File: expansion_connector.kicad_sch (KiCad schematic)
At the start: 18 parts, among them J18 ASP-218650-01_mounting_holes, J8 Plug_Samtec_UMPT_1x6_UMPT-06-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

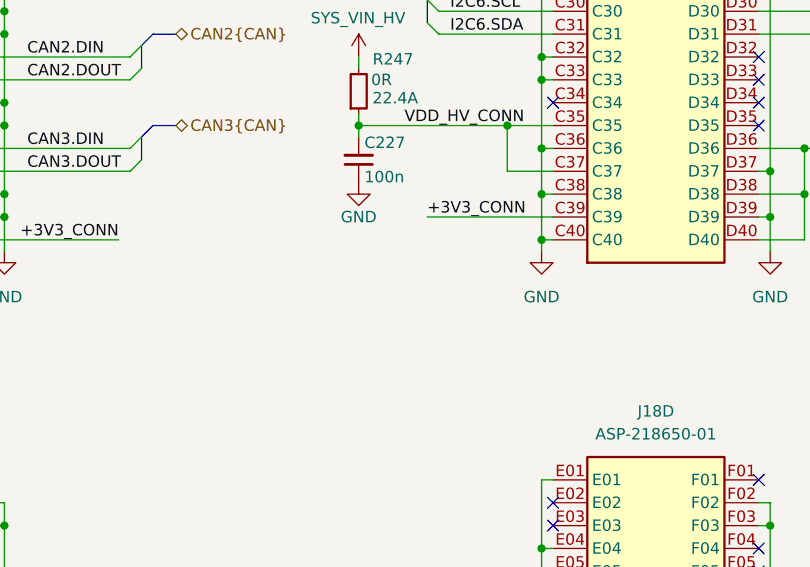
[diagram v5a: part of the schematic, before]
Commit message: [#83396] Implement small post review fixes eg. correct LED resistor values, update sheet table, delete four wire connections
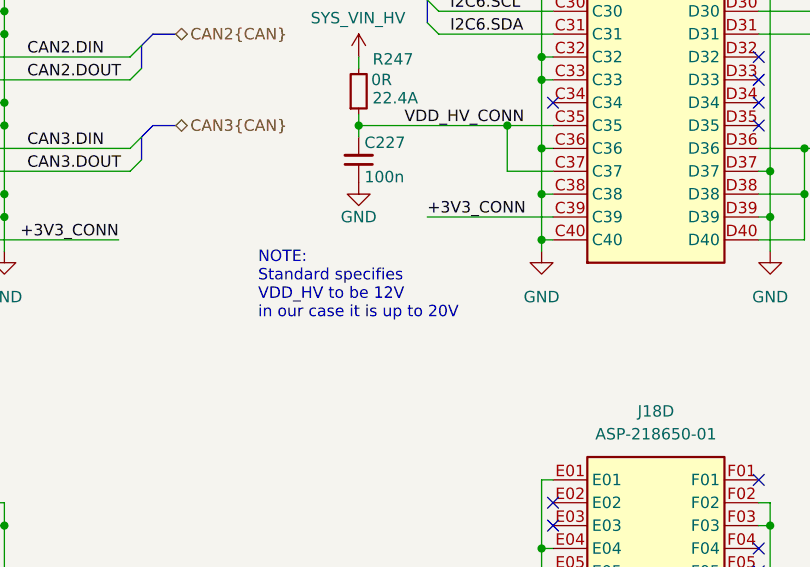
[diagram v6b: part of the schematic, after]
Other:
- note added: "NOTE: Standard specifies VDD_HV to be 12V in our case it is up to 20V"
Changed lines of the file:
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@@
+		)
+	)
+	(text "NOTE:\nStandard specifies\nVDD_HV to be 12V\nin our case it is up to 20V"
+		(exclude_from_sim no)
+		(at 141.224 142.24 0)
+		(effects
+			(font
+				(size 1.27 1.27)
+			)
+			(justify left)
 		)
 	)

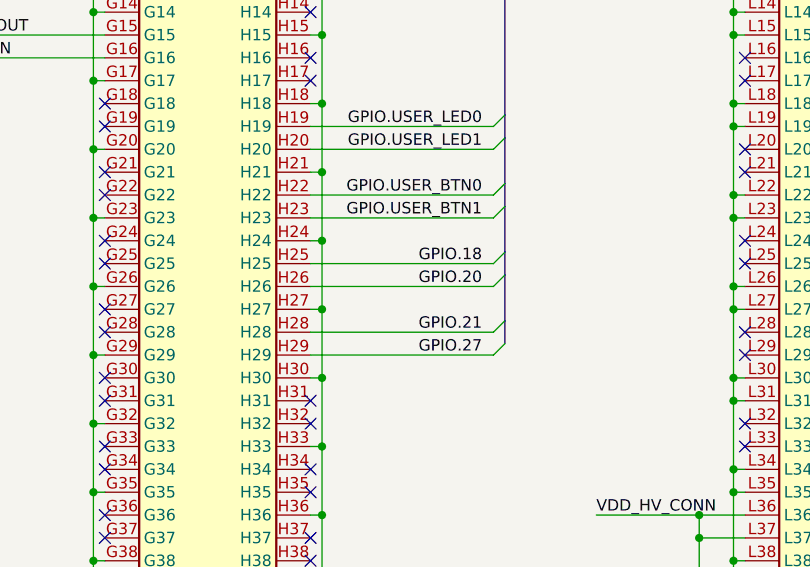
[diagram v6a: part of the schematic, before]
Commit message: [#83396] Continue post review fixes according power and M.2
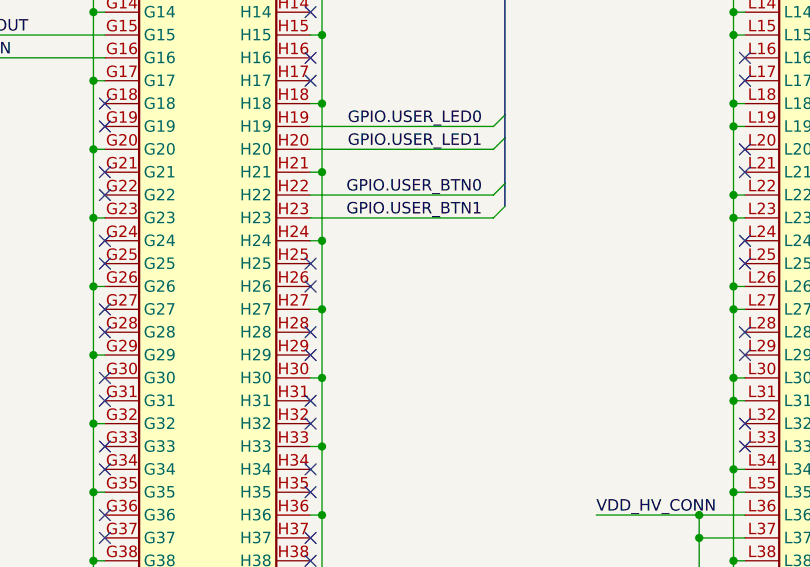
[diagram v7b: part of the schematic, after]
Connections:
- net GPIO.18: no longer names the net of J18.H25
- net GPIO.20: no longer names the net of J18.H26
- net GPIO.21: no longer names the net of J18.H28
- net GPIO.27: no longer names the net of J18.H29
- no-connect marks 201 -> 205
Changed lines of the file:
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@@
 	)
 	(no_connect
+		(at 294.64 99.06)
+	)
+	(no_connect
 		(at 271.78 168.91)
 	)
@@
 	)
 	(no_connect
+		(at 294.64 106.68)
+	)
+	(no_connect
 		(at 111.76 76.2)
 	)
@@
 	)
 	(no_connect
+		(at 294.64 101.6)
+	)
+	(no_connect
 		(at 271.78 207.01)
 	)
@@
 	)
 	(no_connect
+		(at 294.64 109.22)
+	)
+	(no_connect
 		(at 173.99 191.77)
 	)
@@
 	)
 	(bus_entry
-		(at 316.23 107.95)
-		(size -1.27 1.27)
-		(stroke
-			(width 0)
-			(type default)
-		)
-	)
-	(bus_entry
 		(at 215.9 233.68)
 		(size -1.27 1.27)
@@
 	)
 	(bus_entry
-		(at 316.23 105.41)
-		(size -1.27 1.27)
-		(stroke
-			(width 0)
-			(type default)
-		)
-	)
-	(bus_entry
 		(at 250.19 57.15)
 		(size 1.27 1.27)
@@
 	)
 	(bus_entry
-		(at 316.23 97.79)
-		(size -1.27 1.27)
-		(stroke
-			(width 0)
-			(type default)
-		)
-	)
-	(bus_entry
 		(at 134.62 64.77)
 		(size -1.27 1.27)
@@
 	)
 	(bus_entry
-		(at 316.23 100.33)
-		(size -1.27 1.27)
-		(stroke
-			(width 0)
-			(type default)
-		)
-	)
-	(bus_entry
 		(at 35.56 123.19)
 		(size 1.27 1.27)
@@
 		)
 	)
-	(bus
-		(pts
-			(xy 316.23 92.71) (xy 316.23 97.79)
-		)
-		(stroke
-			(width 0)
-			(type default)
-		)
-	)
 	(wire
 		(pts
@@
 		)
 	)
-	(bus
-		(pts
-			(xy 316.23 100.33) (xy 316.23 105.41)
-		)
-		(stroke
-			(width 0)
-			(type default)
-		)
-	)
 	(wire
 		(pts
@@
 		)
 	)
-	(bus
-		(pts
-			(xy 316.23 105.41) (xy 316.23 107.95)
-		)
-		(stroke
-			(width 0)
-			(type default)
-		)
-	)
 	(wire
 		(pts
@@
 		)
 	)
-	(bus
-		(pts
-			(xy 316.23 97.79) (xy 316.23 100.33)
-		)
-		(stroke
-			(width 0)
-			(type default)
-		)
-	)
 	(wire
 		(pts
@@
 	(wire
 		(pts
-			(xy 294.64 106.68) (xy 314.96 106.68)
-		)
-		(stroke
-			(width 0)
-			(type default)
-		)
-	)
-	(wire
-		(pts
 			(xy 196.85 99.06) (xy 198.12 99.06)
 		)
@@
 	(wire
 		(pts
-			(xy 294.64 99.06) (xy 314.96 99.06)
-		)
-		(stroke
-			(width 0)
-			(type default)
-		)
-	)
-	(wire
-		(pts
 			(xy 342.9 101.6) (xy 341.63 101.6)
 		)
@@
 		)
 	)
-	(wire
-		(pts
-			(xy 294.64 101.6) (xy 314.96 101.6)
-		)
-		(stroke
-			(width 0)
-			(type default)
-		)
-	)
 	(bus
 		(pts
@@
 	(wire
 		(pts
-			(xy 294.64 109.22) (xy 314.96 109.22)
-		)
-		(stroke
-			(width 0)
-			(type default)
-		)
-	)
-	(wire
-		(pts
 			(xy 198.12 199.39) (xy 196.85 199.39)
 		)
@@
 		)
 	)
-	(label "GPIO.20"
-		(at 313.69 101.6 180)
-		(effects
-			(font
-				(size 1.27 1.27)
-			)
-			(justify right bottom)
-		)
-	)
 	(label "I2S2.CLK"
 		(at 252.73 50.8 0)
@@
 		)
 	)
-	(label "GPIO.21"
-		(at 313.69 106.68 180)
-		(effects
-			(font
-				(size 1.27 1.27)
-			)
-			(justify right bottom)
-		)
-	)
 	(label "UART5.RTS"
 		(at 200.66 71.12 0)
@@
 		)
 	)
-	(label "GPIO.18"
-		(at 313.69 99.06 180)
-		(effects
-			(font
-				(size 1.27 1.27)
-			)
-			(justify right bottom)
-		)
-	)
 	(label "SPI1.~{CS0}"
 		(at 200.66 201.93 0)
@@
 		)
 	)
-	(label "GPIO.27"
-		(at 313.69 109.22 180)
-		(effects
-			(font
-				(size 1.27 1.27)
-			)
-			(justify right bottom)
-		)
-	)

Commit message: [#83396] Continue post review fixes according USB Hub
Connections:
- net GPIO.18: now reaches J18.H25
- net GPIO.20: now reaches J18.H26
- net GPIO.21: now reaches J18.H28
- net GPIO.27: now reaches J18.H29
- no-connect marks 205 -> 201
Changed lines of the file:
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@@
 	)
 	(no_connect
-		(at 294.64 99.06)
-	)
-	(no_connect
 		(at 271.78 168.91)
 	)
@@
 	)
 	(no_connect
-		(at 294.64 106.68)
-	)
-	(no_connect
 		(at 111.76 76.2)
 	)
@@
 	)
 	(no_connect
-		(at 294.64 101.6)
-	)
-	(no_connect
 		(at 271.78 207.01)
 	)
@@
 	)
 	(no_connect
-		(at 294.64 109.22)
-	)
-	(no_connect
 		(at 173.99 191.77)
 	)
@@
 	)
 	(bus_entry
+		(at 316.23 97.79)
+		(size -1.27 1.27)
+		(stroke
+			(width 0)
+			(type default)
+		)
+	)
+	(bus_entry
 		(at 72.39 248.92)
 		(size 1.27 1.27)
@@
 	)
 	(bus_entry
+		(at 316.23 100.33)
+		(size -1.27 1.27)
+		(stroke
+			(width 0)
+			(type default)
+		)
+	)
+	(bus_entry
 		(at 215.9 208.28)
 		(size -1.27 1.27)
@@
 	)
 	(bus_entry
+		(at 316.23 105.41)
+		(size -1.27 1.27)
+		(stroke
+			(width 0)
+			(type default)
+		)
+	)
+	(bus_entry
 		(at 72.39 259.08)
 		(size 1.27 1.27)
@@
 	)
 	(bus_entry
+		(at 316.23 107.95)
+		(size -1.27 1.27)
+		(stroke
+			(width 0)
+			(type default)
+		)
+	)
+	(bus_entry
 		(at 213.36 113.03)
 		(size -1.27 1.27)
@@
 		)
 	)
+	(bus
+		(pts
+			(xy 316.23 97.79) (xy 316.23 100.33)
+		)
+		(stroke
+			(width 0)
+			(type default)
+		)
+	)
 	(wire
 		(pts
@@
 	(wire
 		(pts
+			(xy 294.64 109.22) (xy 314.96 109.22)
+		)
+		(stroke
+			(width 0)
+			(type default)
+		)
+	)
+	(wire
+		(pts
 			(xy 111.76 66.04) (xy 133.35 66.04)
 		)
@@
 		)
 	)
+	(bus
+		(pts
+			(xy 316.23 92.71) (xy 316.23 97.79)
+		)
+		(stroke
+			(width 0)
+			(type default)
+		)
+	)
 	(wire
 		(pts
@@
 	(wire
 		(pts
+			(xy 294.64 106.68) (xy 314.96 106.68)
+		)
+		(stroke
+			(width 0)
+			(type default)
+		)
+	)
+	(wire
+		(pts
 			(xy 172.72 109.22) (xy 172.72 116.84)
 		)
@@
 	(wire
 		(pts
+			(xy 294.64 99.06) (xy 314.96 99.06)
+		)
+		(stroke
+			(width 0)
+			(type default)
+		)
+	)
+	(wire
+		(pts
 			(xy 127 181.61) (xy 116.84 181.61)
 		)
@@
 		)
 	)
+	(bus
+		(pts
+			(xy 316.23 105.41) (xy 316.23 107.95)
+		)
+		(stroke
+			(width 0)
+			(type default)
+		)
+	)
 	(wire
 		(pts
@@
 		)
 	)
+	(bus
+		(pts
+			(xy 316.23 100.33) (xy 316.23 105.41)
+		)
+		(stroke
+			(width 0)
+			(type default)
+		)
+	)
 	(wire
 		(pts
@@
 	(wire
 		(pts
+			(xy 294.64 101.6) (xy 314.96 101.6)
+		)
+		(stroke
+			(width 0)
+			(type default)
+		)
+	)
+	(wire
+		(pts
 			(xy 198.12 199.39) (xy 196.85 199.39)
 		)
@@
 		)
 	)
+	(label "GPIO.18"
+		(at 313.69 99.06 180)
+		(effects
+			(font
+				(size 1.27 1.27)
+			)
+			(justify right bottom)
+		)
+	)
 	(label "PCIe_{C3x2}.RX0-"
 		(at 38.1 81.28 0)
@@
 		)
 	)
+	(label "GPIO.27"
+		(at 313.69 109.22 180)
+		(effects
+			(font
+				(size 1.27 1.27)
+			)
+			(justify right bottom)
+		)
+	)
 	(label "SPI3.~{CS1}"
 		(at 200.66 242.57 0)
@@
 		)
 	)
+	(label "GPIO.20"
+		(at 313.69 101.6 180)
+		(effects
+			(font
+				(size 1.27 1.27)
+			)
+			(justify right bottom)
+		)
+	)
 	(label "+3V3_CONN"
 		(at 351.79 223.52 180)
@@
 		)
 	)
+	(label "GPIO.21"
+		(at 313.69 106.68 180)
+		(effects
+			(font
+				(size 1.27 1.27)
+			)
+			(justify right bottom)
+		)
+	)
